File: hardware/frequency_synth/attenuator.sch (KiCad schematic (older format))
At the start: 33 parts, among them U401 LTC1983, U402 HMC424, U403 74HC04_FULL

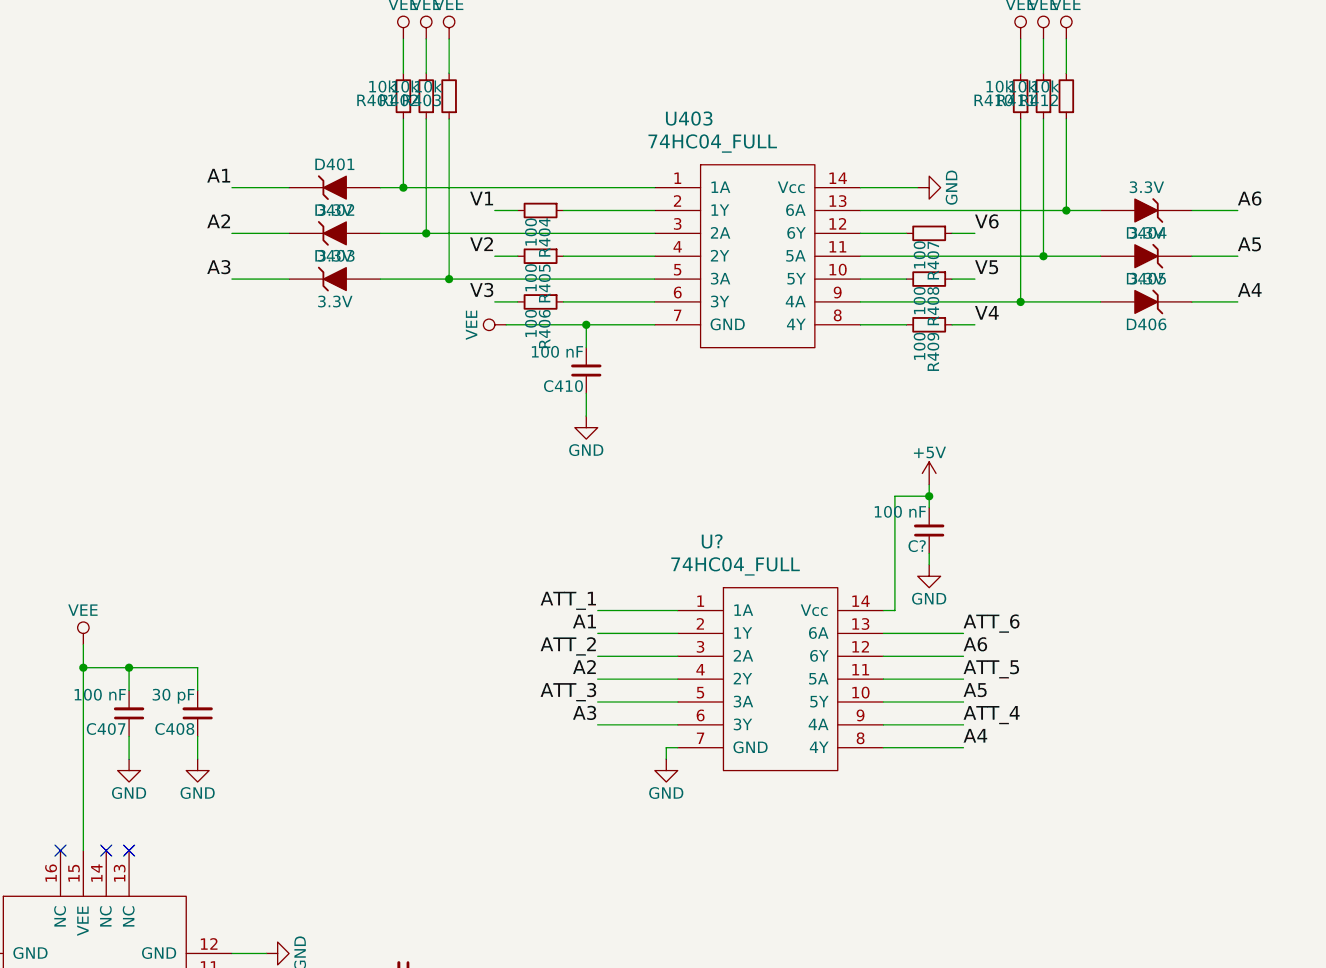
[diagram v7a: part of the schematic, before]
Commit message: finished layout of r1 synth board (switched to cpw sma, added test points, fixed r0 errata, removed power detector and amp (make separate board))
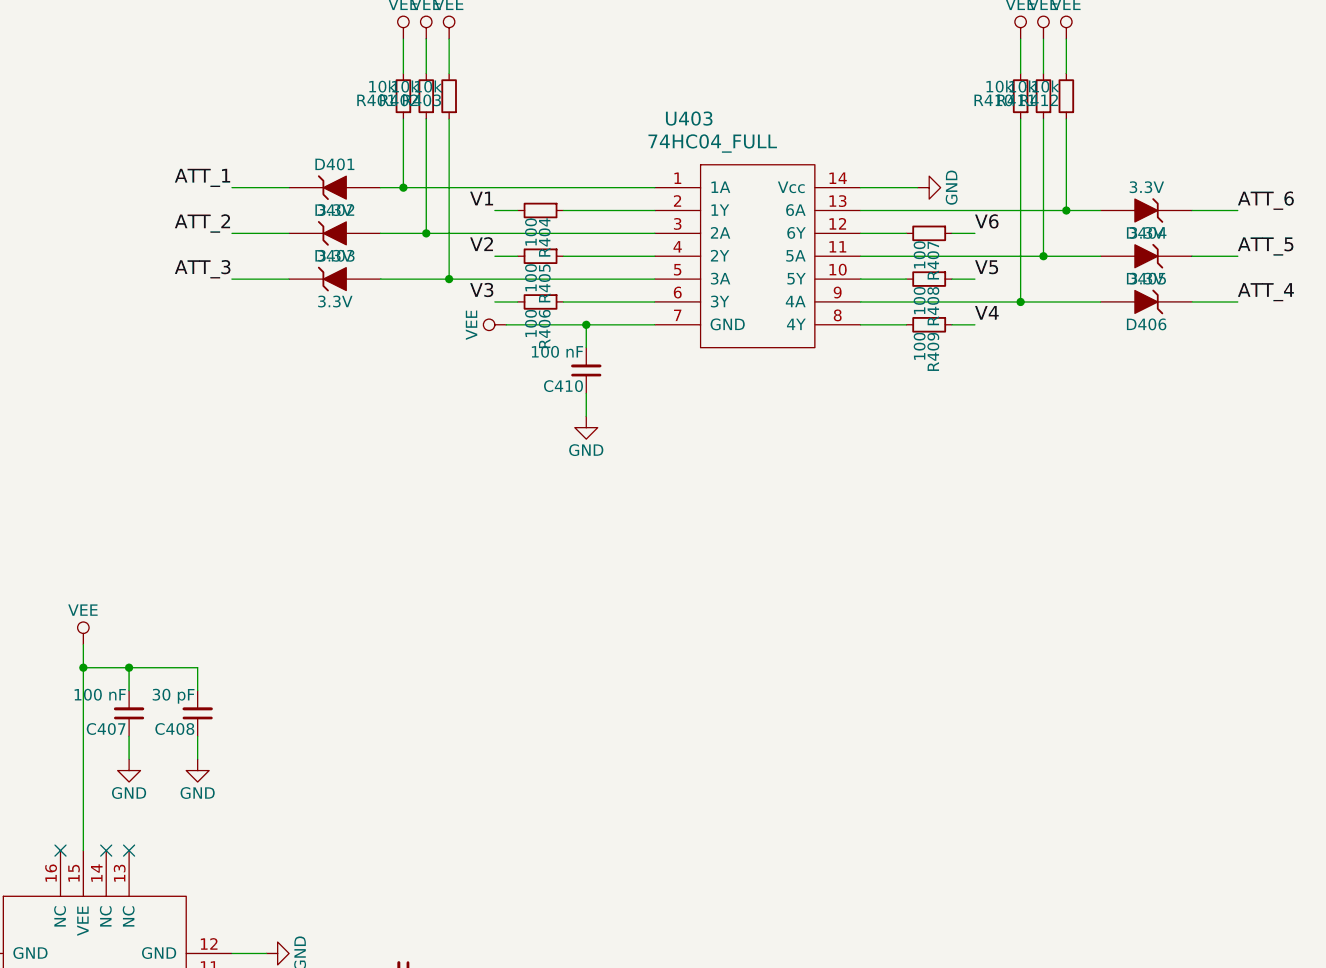
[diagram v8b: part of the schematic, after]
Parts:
- removed C?: 100 nF, Capacitors_SMD:C_0402, symbol C_Small
- removed U?: 74HC04_FULL, Housings_SSOP:TSSOP-14_4.4x5mm_Pitch0.65mm, symbol 74HC04_FULL
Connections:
- net A1 is gone; now on net ATT_A1: D401.1 (K)
- net A2 is gone; now on net ATT_A2: D402.1 (K)
- net A3 is gone; now on net ATT_A3: D403.1 (K)
- net A4 is gone; now on net ATT_A4: D406.1 (K)
- net A5 is gone; now on net ATT_A5: D405.1 (K)
- net A6 is gone; now on net ATT_A6: D404.1 (K)
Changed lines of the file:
@@
 $Descr A4 11693 8268
 encoding utf-8
-Sheet 4 9
+Sheet 4 8
 Title ""
 Date ""
@@
 $EndComp
 $Comp
-L GND #PWR0108
+L GND #PWR0107
 U 1 1 572AE6C7
 P 8800 1800
-F 0 "#PWR0108" H 8800 1550 50  0001 C CNN
+F 0 "#PWR0107" H 8800 1550 50  0001 C CNN
 F 1 "GND" H 8800 1650 50  0000 C CNN
 F 2 "" H 8800 1800 50  0000 C CNN
@@
 	8800 1800 8550 1800
 $Comp
-L VEE #PWR0109
+L VEE #PWR0108
 U 1 1 572AE6C8
 P 7000 2400
-F 0 "#PWR0109" H 7000 2250 50  0001 C CNN
+F 0 "#PWR0108" H 7000 2250 50  0001 C CNN
 F 1 "VEE" H 7000 2550 50  0000 C CNN
 F 2 "" H 7000 2400 50  0000 C CNN
@@
 $EndComp
 $Comp
-L GND #PWR0110
+L GND #PWR0109
 U 1 1 572AE6CA
 P 7350 2800
-F 0 "#PWR0110" H 7350 2550 50  0001 C CNN
+F 0 "#PWR0109" H 7350 2550 50  0001 C CNN
 F 1 "GND" H 7350 2650 50  0000 C CNN
 F 2 "" H 7350 2800 50  0000 C CNN
@@
 	9450 1300 9450 1150
 $Comp
-L VEE #PWR0111
+L VEE #PWR0110
 U 1 1 572AE6D7
 P 6550 1150
-F 0 "#PWR0111" H 6550 1000 50  0001 C CNN
+F 0 "#PWR0110" H 6550 1000 50  0001 C CNN
 F 1 "VEE" H 6550 1300 50  0000 C CNN
 F 2 "" H 6550 1150 50  0000 C CNN
@@
 $EndComp
 $Comp
-L VEE #PWR0112
+L VEE #PWR0111
 U 1 1 572AE6D8
 P 6650 1150
-F 0 "#PWR0112" H 6650 1000 50  0001 C CNN
+F 0 "#PWR0111" H 6650 1000 50  0001 C CNN
 F 1 "VEE" H 6650 1300 50  0000 C CNN
 F 2 "" H 6650 1150 50  0000 C CNN
@@
 $EndComp
 $Comp
-L VEE #PWR0113
+L VEE #PWR0112
 U 1 1 572AE6D9
 P 6750 1150
-F 0 "#PWR0113" H 6750 1000 50  0001 C CNN
+F 0 "#PWR0112" H 6750 1000 50  0001 C CNN
 F 1 "VEE" H 6750 1300 50  0000 C CNN
 F 2 "" H 6750 1150 50  0000 C CNN
@@
 $EndComp
 $Comp
-L VEE #PWR0114
+L VEE #PWR0113
 U 1 1 572AE6DA
 P 9250 1150
-F 0 "#PWR0114" H 9250 1000 50  0001 C CNN
+F 0 "#PWR0113" H 9250 1000 50  0001 C CNN
 F 1 "VEE" H 9250 1300 50  0000 C CNN
 F 2 "" H 9250 1150 50  0000 C CNN
@@
 $EndComp
 $Comp
-L VEE #PWR0115
+L VEE #PWR0114
 U 1 1 572AE6DB
 P 9350 1150
-F 0 "#PWR0115" H 9350 1000 50  0001 C CNN
+F 0 "#PWR0114" H 9350 1000 50  0001 C CNN
 F 1 "VEE" H 9350 1300 50  0000 C CNN
 F 2 "" H 9350 1150 50  0000 C CNN
@@
 $EndComp
 $Comp
-L VEE #PWR0116
+L VEE #PWR0115
 U 1 1 572AE6DC
 P 9450 1150
-F 0 "#PWR0116" H 9450 1000 50  0001 C CNN
+F 0 "#PWR0115" H 9450 1000 50  0001 C CNN
 F 1 "VEE" H 9450 1300 50  0000 C CNN
 F 2 "" H 9450 1150 50  0000 C CNN
@@
 Wire Wire Line
 	10000 2300 10200 2300
-Text Label 5800 1800 2    60   ~ 0
-A1
-Text Label 5800 2000 2    60   ~ 0
-A2
-Text Label 5800 2200 2    60   ~ 0
-A3
-Text Label 10200 1900 0    60   ~ 0
-A6
-Text Label 10200 2100 0    60   ~ 0
-A5
-Text Label 10200 2300 0    60   ~ 0
-A4
 Wire Wire Line
 	6650 5250 6850 5250
@@
 	5800 5250 6450 5250
 $Comp
-L GND #PWR0117
+L GND #PWR0116
 U 1 1 572AE6DF
 P 5950 5150
-F 0 "#PWR0117" H 5950 4900 50  0001 C CNN
+F 0 "#PWR0116" H 5950 4900 50  0001 C CNN
 F 1 "GND" H 5950 5000 50  0000 C CNN
 F 2 "" H 5950 5150 50  0000 C CNN
@@
 	5950 5150 5800 5150
 $Comp
-L GND #PWR0118
+L GND #PWR0117
 U 1 1 572AE6E0
 P 5950 5350
-F 0 "#PWR0118" H 5950 5100 50  0001 C CNN
+F 0 "#PWR0117" H 5950 5100 50  0001 C CNN
 F 1 "GND" H 5950 5200 50  0000 C CNN
 F 2 "" H 5950 5350 50  0000 C CNN
@@
 	5950 5350 5800 5350
 $Comp
-L GND #PWR0119
+L GND #PWR0118
 U 1 1 572AE6E1
 P 5450 6050
-F 0 "#PWR0119" H 5450 5800 50  0001 C CNN
+F 0 "#PWR0118" H 5450 5800 50  0001 C CNN
 F 1 "GND" H 5450 5900 50  0000 C CNN
 F 2 "" H 5450 6050 50  0000 C CNN
@@
 	5450 6050 5450 5900
 $Comp
-L GND #PWR0120
+L GND #PWR0119
 U 1 1 572AE6E2
 P 4450 5350
-F 0 "#PWR0120" H 4450 5100 50  0001 C CNN
+F 0 "#PWR0119" H 4450 5100 50  0001 C CNN
 F 1 "GND" H 4450 5200 50  0000 C CNN
 F 2 "" H 4450 5350 50  0000 C CNN
@@
 $EndComp
 $Comp
-L GND #PWR0121
+L GND #PWR0120
 U 1 1 572AE6E3
 P 4450 5150
-F 0 "#PWR0121" H 4450 4900 50  0001 C CNN
+F 0 "#PWR0120" H 4450 4900 50  0001 C CNN
 F 1 "GND" H 4450 5000 50  0000 C CNN
 F 2 "" H 4450 5150 50  0000 C CNN
@@
 	4450 5350 4600 5350
 $Comp
-L VEE #PWR0122
+L VEE #PWR0121
 U 1 1 572AE6E4
 P 5150 3800
-F 0 "#PWR0122" H 5150 3650 50  0001 C CNN
+F 0 "#PWR0121" H 5150 3650 50  0001 C CNN
 F 1 "VEE" H 5150 3950 50  0000 C CNN
 F 2 "" H 5150 3800 50  0000 C CNN
@@
 $EndComp
 $Comp
-L GND #PWR0123
+L GND #PWR0122
 U 1 1 572AE6E6
 P 5350 4300
-F 0 "#PWR0123" H 5350 4050 50  0001 C CNN
+F 0 "#PWR0122" H 5350 4050 50  0001 C CNN
 F 1 "GND" H 5350 4150 50  0000 C CNN
 F 2 "" H 5350 4300 50  0000 C CNN
@@
 	5050 5900 5050 6350
 $Comp
-L GND #PWR0124
+L GND #PWR0123
 U 1 1 572AE6E8
 P 1200 4050
-F 0 "#PWR0124" H 1200 3800 50  0001 C CNN
+F 0 "#PWR0123" H 1200 3800 50  0001 C CNN
 F 1 "GND" H 1200 3900 50  0000 C CNN
 F 2 "" H 1200 4050 50  0000 C CNN
@@
 $EndComp
 $Comp
-L +5V #PWR0125
+L +5V #PWR0124
 U 1 1 572AE6EA
 P 1450 3850
-F 0 "#PWR0125" H 1450 3700 50  0001 C CNN
+F 0 "#PWR0124" H 1450 3700 50  0001 C CNN
 F 1 "+5V" H 1450 3990 50  0000 C CNN
 F 2 "" H 1450 3850 50  0000 C CNN
@@
 	1450 3850 1100 3850
 $Comp
-L VEE #PWR0126
+L VEE #PWR0125
 U 1 1 572AE6EB
 P 1250 2450
-F 0 "#PWR0126" H 1250 2300 50  0001 C CNN
+F 0 "#PWR0125" H 1250 2300 50  0001 C CNN
 F 1 "VEE" H 1250 2600 50  0000 C CNN
 F 2 "" H 1250 2450 50  0000 C CNN
@@
 $EndComp
 $Comp
-L +5V #PWR0127
+L +5V #PWR0126
 U 1 1 572AE6EC
 P 2150 1600
-F 0 "#PWR0127" H 2150 1450 50  0001 C CNN
+F 0 "#PWR0126" H 2150 1450 50  0001 C CNN
 F 1 "+5V" H 2150 1740 50  0000 C CNN
 F 2 "" H 2150 1600 50  0000 C CNN
@@
 	3550 2550 3450 2550
 $Comp
-L GND #PWR0128
+L GND #PWR0127
 U 1 1 572AE6EE
 P 3600 2450
-F 0 "#PWR0128" H 3600 2200 50  0001 C CNN
+F 0 "#PWR0127" H 3600 2200 50  0001 C CNN
 F 1 "GND" H 3600 2300 50  0000 C CNN
 F 2 "" H 3600 2450 50  0000 C CNN
@@
 $EndComp
 $Comp
-L GND #PWR0129
+L GND #PWR0128
 U 1 1 572AE6F0
 P 1900 2900
-F 0 "#PWR0129" H 1900 2650 50  0001 C CNN
+F 0 "#PWR0128" H 1900 2650 50  0001 C CNN
 F 1 "GND" H 1900 2750 50  0000 C CNN
 F 2 "" H 1900 2900 50  0000 C CNN
@@
 Connection ~ 1900 2450
 $Comp
-L GND #PWR0130
+L GND #PWR0129
 U 1 1 572AE6F1
 P 1900 2200
-F 0 "#PWR0130" H 1900 1950 50  0001 C CNN
+F 0 "#PWR0129" H 1900 1950 50  0001 C CNN
 F 1 "GND" H 1900 2050 50  0000 C CNN
 F 2 "" H 1900 2200 50  0000 C CNN
@@
 $EndComp
 $Comp
-L GND #PWR0131
+L GND #PWR0130
 U 1 1 572AE6F4
 P 1650 2200
-F 0 "#PWR0131" H 1650 1950 50  0001 C CNN
+F 0 "#PWR0130" H 1650 1950 50  0001 C CNN
 F 1 "GND" H 1650 2050 50  0000 C CNN
 F 2 "" H 1650 2200 50  0000 C CNN
@@
 $EndComp
 $Comp
-L GND #PWR0132
+L GND #PWR0131
 U 1 1 572AE6F6
 P 5650 4300
-F 0 "#PWR0132" H 5650 4050 50  0001 C CNN
+F 0 "#PWR0131" H 5650 4050 50  0001 C CNN
 F 1 "GND" H 5650 4150 50  0000 C CNN
 F 2 "" H 5650 4300 50  0000 C CNN
@@
 $EndComp
 $Comp
-L GND #PWR0133
+L GND #PWR0132
 U 1 1 572AE6F8
 P 1350 2200
-F 0 "#PWR0133" H 1350 1950 50  0001 C CNN
+F 0 "#PWR0132" H 1350 1950 50  0001 C CNN
 F 1 "GND" H 1350 2050 50  0000 C CNN
 F 2 "" H 1350 2200 50  0000 C CNN
@@
 Wire Wire Line
 	3250 5250 3600 5250
-$Comp
-L 74HC04_FULL U?
-U 1 1 57C3BD51
-P 8200 3950
-F 0 "U?" H 7900 4550 60  0000 C CNN
-F 1 "74HC04_FULL" H 8000 4450 60  0000 C CNN
-F 2 "Housings_SSOP:TSSOP-14_4.4x5mm_Pitch0.65mm" H 8200 3950 60  0001 C CNN
-F 3 "" H 8200 3950 60  0000 C CNN
-	1    8200 3950
-	1    0    0    -1
-$EndComp
-$Comp
-L C_Small C?
-U 1 1 57C3BF75
-P 8850 3300
-F 0 "C?" H 8860 3370 50  0000 L CNN
-F 1 "100 nF" H 8860 3220 50  0000 L CNN
-F 2 "Capacitors_SMD:C_0402" H 8850 3300 50  0001 C CNN
-F 3 "" H 8850 3300 50  0000 C CNN
-	1    8850 3300
-	-1   0    0    1
-$EndComp
-$Comp
-L GND #PWR?
-U 1 1 57C3C099
-P 8850 3450
-F 0 "#PWR?" H 8850 3200 50  0001 C CNN
-F 1 "GND" H 8850 3300 50  0000 C CNN
-F 2 "" H 8850 3450 50  0000 C CNN
-F 3 "" H 8850 3450 50  0000 C CNN
-	1    8850 3450
-	1    0    0    -1
-$EndComp
-Wire Wire Line
-	8850 3400 8850 3450
-$Comp
-L +5V #PWR?
-U 1 1 57C3C52B
-P 8850 3100
-F 0 "#PWR?" H 8850 2950 50  0001 C CNN
-F 1 "+5V" H 8850 3240 50  0000 C CNN
-F 2 "" H 8850 3100 50  0000 C CNN
-F 3 "" H 8850 3100 50  0000 C CNN
-	1    8850 3100
-	1    0    0    -1
-$EndComp
-Wire Wire Line
-	8850 3100 8850 3200
-Wire Wire Line
-	8850 3150 8700 3150
-Wire Wire Line
-	8700 3150 8700 3650
-Wire Wire Line
-	8700 3650 8650 3650
-Connection ~ 8850 3150
-$Comp
-L GND #PWR?
-U 1 1 57C3CA74
-P 7700 4300
-F 0 "#PWR?" H 7700 4050 50  0001 C CNN
-F 1 "GND" H 7700 4150 50  0000 C CNN
-F 2 "" H 7700 4300 50  0000 C CNN
-F 3 "" H 7700 4300 50  0000 C CNN
-	1    7700 4300
-	1    0    0    -1
-$EndComp
-Wire Wire Line
-	7750 4250 7700 4250
-Wire Wire Line
-	7700 4250 7700 4300
-Text Label 7400 3750 2    60   ~ 0
-A1
-Wire Wire Line
-	7400 3750 7750 3750
-Wire Wire Line
-	7400 3650 7750 3650
-Text Label 7400 3650 2    60   ~ 0
+Text Label 10200 1900 0    60   ~ 0
+ATT_6
+Text Label 10200 2100 0    60   ~ 0
+ATT_5
+Text Label 10200 2300 0    60   ~ 0
+ATT_4
+Text Label 5800 1800 2    60   ~ 0
 ATT_1
-Text Label 7400 3850 2    60   ~ 0
+Text Label 5800 2000 2    60   ~ 0
 ATT_2
-Wire Wire Line
-	7400 3850 7750 3850
-Text Label 7400 3950 2    60   ~ 0
-A2
-Wire Wire Line
-	7400 3950 7750 3950
-Text Label 7400 4050 2    60   ~ 0
+Text Label 5800 2200 2    60   ~ 0
 ATT_3
-Text Label 7400 4150 2    60   ~ 0
-A3
-Wire Wire Line
-	7400 4150 7750 4150
-Wire Wire Line
-	7400 4050 7750 4050
-Text Label 9000 3850 0    60   ~ 0
-A6
-Wire Wire Line
-	9000 3850 8650 3850
-Wire Wire Line
-	9000 3750 8650 3750
-Text Label 9000 3750 0    60   ~ 0
-ATT_6
-Text Label 9000 3950 0    60   ~ 0
-ATT_5
-Wire Wire Line
-	9000 3950 8650 3950
-Text Label 9000 4050 0    60   ~ 0
-A5
-Wire Wire Line
-	9000 4050 8650 4050
-Text Label 9000 4150 0    60   ~ 0
-ATT_4
-Text Label 9000 4250 0    60   ~ 0
-A4
-Wire Wire Line
-	9000 4250 8650 4250
-Wire Wire Line
-	9000 4150 8650 4150
 $EndSCHEMATC
